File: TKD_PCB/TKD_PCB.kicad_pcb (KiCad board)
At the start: 2 copper layers, 83.8 x 53.3 mm, 3 parts, among them U1 ESP32-WROOM-32D

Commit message: Begin of the final assembly
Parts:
- removed D1, D3: LED, LED_THT:LED_D3.0mm
- removed U1: ESP32-WROOM-32D, RF_Module:ESP32-WROOM-32
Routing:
- net GND: track 35.9 -> 0.00 mm
- removed copper zone on F.Cu, net GND
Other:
- board outline removed

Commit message: did Remco's homework
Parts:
- added C1: 100nF, Capacitor_SMD:C_0805_2012Metric_Pad1.15x1.40mm_HandSolder, F.Cu at (38.5, 125.3)
- added C10: 100nF, Capacitor_SMD:C_0805_2012Metric_Pad1.15x1.40mm_HandSolder, F.Cu at (156.2, 102.5)
- added C11: 10uF, Capacitor_SMD:C_0805_2012Metric_Pad1.15x1.40mm_HandSolder, F.Cu at (150.5, 95.8)
- added C12: 100nF, Capacitor_SMD:C_0805_2012Metric_Pad1.15x1.40mm_HandSolder, F.Cu at (59.4, 147.7)
- added C13: 100nF, Capacitor_SMD:C_0805_2012Metric_Pad1.15x1.40mm_HandSolder, F.Cu at (59.5, 144.6)
- added C14: 100nF, Capacitor_SMD:C_0805_2012Metric_Pad1.15x1.40mm_HandSolder, F.Cu at (58.7, 169.2)
- added C15: 100nF, Capacitor_SMD:C_0805_2012Metric_Pad1.15x1.40mm_HandSolder, F.Cu at (48.4, 163.3)
- added C16: 100nF, Capacitor_SMD:C_0805_2012Metric_Pad1.15x1.40mm_HandSolder, F.Cu at (39.9, 154.8)
- added C17: 100nF, Capacitor_SMD:C_0805_2012Metric_Pad1.15x1.40mm_HandSolder, F.Cu at (34.0, 144.5)
- added C18: 100nF, Capacitor_SMD:C_0805_2012Metric_Pad1.15x1.40mm_HandSolder, F.Cu at (30.9, 133.0)
- added C19: 100nF, Capacitor_SMD:C_0805_2012Metric_Pad1.15x1.40mm_HandSolder, F.Cu at (30.9, 121.0)
- added C2: 10uF, Capacitor_SMD:C_0805_2012Metric_Pad1.15x1.40mm_HandSolder, F.Cu at (38.5, 127.7)
- added C20: 100nF, Capacitor_SMD:C_0805_2012Metric_Pad1.15x1.40mm_HandSolder, F.Cu at (34.0, 109.5)
- added C21: 100nF, Capacitor_SMD:C_0805_2012Metric_Pad1.15x1.40mm_HandSolder, F.Cu at (39.9, 99.2)
- added C22: 100nF, Capacitor_SMD:C_0805_2012Metric_Pad1.15x1.40mm_HandSolder, F.Cu at (48.4, 90.7)
- added C23: 100nF, Capacitor_SMD:C_0805_2012Metric_Pad1.15x1.40mm_HandSolder, F.Cu at (58.7, 84.8)
- added C24: 100nF, Capacitor_SMD:C_0805_2012Metric_Pad1.15x1.40mm_HandSolder, F.Cu at (70.2, 81.7)
- added C25: 100nF, Capacitor_SMD:C_0805_2012Metric_Pad1.15x1.40mm_HandSolder, F.Cu at (82.2, 81.7)
- added C26: 100nF, Capacitor_SMD:C_0805_2012Metric_Pad1.15x1.40mm_HandSolder, F.Cu at (93.7, 84.8)
- added C27: 100nF, Capacitor_SMD:C_0805_2012Metric_Pad1.15x1.40mm_HandSolder, F.Cu at (104.0, 90.7)
- added C28: 100nF, Capacitor_SMD:C_0805_2012Metric_Pad1.15x1.40mm_HandSolder, F.Cu at (112.5, 99.2)
- added C29: 100nF, Capacitor_SMD:C_0805_2012Metric_Pad1.15x1.40mm_HandSolder, F.Cu at (118.4, 109.5)
- added C3: 10uF, Capacitor_SMD:C_0805_2012Metric_Pad1.15x1.40mm_HandSolder, F.Cu at (89.8, 145.7)
- added C30: 100nF, Capacitor_SMD:C_0805_2012Metric_Pad1.15x1.40mm_HandSolder, F.Cu at (121.5, 121.0)
- added C31: 100nF, Capacitor_SMD:C_0805_2012Metric_Pad1.15x1.40mm_HandSolder, F.Cu at (121.5, 133.0)
- added C32: 100nF, Capacitor_SMD:C_0805_2012Metric_Pad1.15x1.40mm_HandSolder, F.Cu at (118.4, 144.5)
- added C33: 100nF, Capacitor_SMD:C_0805_2012Metric_Pad1.15x1.40mm_HandSolder, F.Cu at (112.5, 154.8)
- added C34: 100nF, Capacitor_SMD:C_0805_2012Metric_Pad1.15x1.40mm_HandSolder, F.Cu at (104.0, 163.3)
- added C35: 100nF, Capacitor_SMD:C_0805_2012Metric_Pad1.15x1.40mm_HandSolder, F.Cu at (93.7, 169.2)
- added C36: 100nF, Capacitor_SMD:C_0805_2012Metric_Pad1.15x1.40mm_HandSolder, F.Cu at (82.2, 172.3)
- added C37: 100nF, Capacitor_SMD:C_0805_2012Metric_Pad1.15x1.40mm_HandSolder, F.Cu at (70.2, 172.3)
- added C4: 100nF, Capacitor_SMD:C_0805_2012Metric_Pad1.15x1.40mm_HandSolder, F.Cu at (89.7, 143.4)
- added C5: 100nF, Capacitor_SMD:C_0805_2012Metric_Pad1.15x1.40mm_HandSolder, F.Cu at (89.6, 148.8)
- added C6: 10uF, Capacitor_SMD:C_0805_2012Metric_Pad1.15x1.40mm_HandSolder, F.Cu at (89.6, 151.9)
- added C7: 100nF, Capacitor_SMD:C_0805_2012Metric_Pad1.15x1.40mm_HandSolder, F.Cu at (59.6, 141.3)
- added C8: 10uF, Capacitor_SMD:C_0805_2012Metric_Pad1.15x1.40mm_HandSolder, F.Cu at (155.8, 98.2)
- added C9: 100nF, Capacitor_SMD:C_0805_2012Metric_Pad1.15x1.40mm_HandSolder, F.Cu at (89.7, 139.8)
- added D1: D, Diode_SMD:D_0805_2012Metric_Pad1.15x1.40mm_HandSolder, F.Cu at (100.1, 151.2)
- added D10: WS2812B, LED_SMD:LED_WS2812B_PLCC4_5.0x5.0mm_P3.2mm, F.Cu at (43.9, 159.3)
- added D11: WS2812B, LED_SMD:LED_WS2812B_PLCC4_5.0x5.0mm_P3.2mm, F.Cu at (36.6, 149.9)
- added D12: WS2812B, LED_SMD:LED_WS2812B_PLCC4_5.0x5.0mm_P3.2mm, F.Cu at (32.0, 138.8)
- added D13: WS2812B, LED_SMD:LED_WS2812B_PLCC4_5.0x5.0mm_P3.2mm, F.Cu at (30.5, 127.0)
- added D14: WS2812B, LED_SMD:LED_WS2812B_PLCC4_5.0x5.0mm_P3.2mm, F.Cu at (32.0, 115.2)
- added D15: WS2812B, LED_SMD:LED_WS2812B_PLCC4_5.0x5.0mm_P3.2mm, F.Cu at (36.6, 104.1)
- added D16: WS2812B, LED_SMD:LED_WS2812B_PLCC4_5.0x5.0mm_P3.2mm, F.Cu at (43.9, 94.7)
- added D17: WS2812B, LED_SMD:LED_WS2812B_PLCC4_5.0x5.0mm_P3.2mm, F.Cu at (53.3, 87.4)
- added D18: WS2812B, LED_SMD:LED_WS2812B_PLCC4_5.0x5.0mm_P3.2mm, F.Cu at (64.4, 82.8)
- added D19: WS2812B, LED_SMD:LED_WS2812B_PLCC4_5.0x5.0mm_P3.2mm, F.Cu at (76.2, 81.3)
- added D2: D, Diode_SMD:D_SOD-123, F.Cu at (38.7, 119.8)
- added D20: WS2812B, LED_SMD:LED_WS2812B_PLCC4_5.0x5.0mm_P3.2mm, F.Cu at (88.0, 82.8)
- added D21: WS2812B, LED_SMD:LED_WS2812B_PLCC4_5.0x5.0mm_P3.2mm, F.Cu at (99.1, 87.4)
- added D22: WS2812B, LED_SMD:LED_WS2812B_PLCC4_5.0x5.0mm_P3.2mm, F.Cu at (108.5, 94.7)
- added D23: WS2812B, LED_SMD:LED_WS2812B_PLCC4_5.0x5.0mm_P3.2mm, F.Cu at (115.8, 104.1)
- added D24: WS2812B, LED_SMD:LED_WS2812B_PLCC4_5.0x5.0mm_P3.2mm, F.Cu at (120.4, 115.2)
- added D25: WS2812B, LED_SMD:LED_WS2812B_PLCC4_5.0x5.0mm_P3.2mm, F.Cu at (121.9, 127.0)
- added D26: WS2812B, LED_SMD:LED_WS2812B_PLCC4_5.0x5.0mm_P3.2mm, F.Cu at (120.4, 138.8)
- added D27: WS2812B, LED_SMD:LED_WS2812B_PLCC4_5.0x5.0mm_P3.2mm, F.Cu at (115.8, 149.9)
- added D28: WS2812B, LED_SMD:LED_WS2812B_PLCC4_5.0x5.0mm_P3.2mm, F.Cu at (108.5, 159.3)
- added D29: WS2812B, LED_SMD:LED_WS2812B_PLCC4_5.0x5.0mm_P3.2mm, F.Cu at (99.1, 166.6)
- added D3: LED, Diode_SMD:D_0805_2012Metric_Pad1.15x1.40mm_HandSolder, F.Cu at (95.6, 155.2)
- added D30: WS2812B, LED_SMD:LED_WS2812B_PLCC4_5.0x5.0mm_P3.2mm, F.Cu at (88.0, 171.2)
- added D4: D, Diode_SMD:D_0805_2012Metric_Pad1.15x1.40mm_HandSolder, F.Cu at (155.5, 88.4)
- added D5: LED, Diode_SMD:D_0805_2012Metric_Pad1.15x1.40mm_HandSolder, F.Cu at (156.4, 93.1)
- added D6: D, Diode_SMD:D_0805_2012Metric_Pad1.15x1.40mm_HandSolder, F.Cu at (59.4, 136.5)
- added D7: WS2812B, LED_SMD:LED_WS2812B_PLCC4_5.0x5.0mm_P3.2mm, F.Cu at (76.2, 172.7)
- added D8: WS2812B, LED_SMD:LED_WS2812B_PLCC4_5.0x5.0mm_P3.2mm, F.Cu at (64.4, 171.2)
- added D9: WS2812B, LED_SMD:LED_WS2812B_PLCC4_5.0x5.0mm_P3.2mm, F.Cu at (53.3, 166.6)
- added IC1: R5460N233AF-TR-FE, SamacSys_Parts:SOT95P280X140-6N, F.Cu at (54.1, 143.5)
- added J2: Conn_01x06, Connector_PinSocket_2.54mm:PinSocket_1x06_P2.54mm_Vertical, F.Cu at (84.1, 124.5)
- added J3: Conn_02x02_Top_Bottom, Connector_PinHeader_2.54mm:PinHeader_2x02_P2.54mm_Vertical, F.Cu at (54.8, 96.5)
- added J4: Conn_01x07, Connector_PinSocket_2.54mm:PinSocket_1x07_P2.54mm_Vertical, F.Cu at (99.0, 100.2)
- added J5: Conn_01x08, Connector_PinSocket_2.54mm:PinSocket_1x08_P2.54mm_Vertical, F.Cu at (60.8, 100.2)
- added Q1: ZXMN6A09GQTA, SamacSys_Parts:SOT230P700X165-4N, F.Cu at (45.1, 145.6)
- added Q2: ZXMN6A09GQTA, SamacSys_Parts:SOT230P700X165-4N, F.Cu at (45.1, 138.5)
- added Q3: S8050, Package_TO_SOT_THT:TO-92_Inline, F.Cu at (54.4, 125.0)
- added Q4: S8050, Package_TO_SOT_THT:TO-92_Inline, F.Cu at (54.5, 132.2)
- added R1: 22R, Resistor_SMD:R_0805_2012Metric_Pad1.15x1.40mm_HandSolder, F.Cu at (55.5, 116.7)
- added R10: 12k, Resistor_SMD:R_0805_2012Metric_Pad1.15x1.40mm_HandSolder, F.Cu at (55.4, 128.3)
- added R11: 10k, Resistor_SMD:R_0805_2012Metric_Pad1.15x1.40mm_HandSolder, F.Cu at (60.8, 126.3)
- added R12: 5k, Resistor_SMD:R_0805_2012Metric_Pad1.15x1.40mm_HandSolder, F.Cu at (89.7, 121.0)
- added R2: 1k, Resistor_SMD:R_0805_2012Metric_Pad1.15x1.40mm_HandSolder, F.Cu at (95.8, 151.7)
- added R3: 22R, Resistor_SMD:R_0805_2012Metric_Pad1.15x1.40mm_HandSolder, F.Cu at (55.5, 118.7)
- added R4: 330R, Resistor_SMD:R_0805_2012Metric_Pad1.15x1.40mm_HandSolder, F.Cu at (59.5, 138.7)
- added R5: 1k, Resistor_SMD:R_0805_2012Metric_Pad1.15x1.40mm_HandSolder, F.Cu at (54.1, 147.7)
- added R6: 330R, Resistor_SMD:R_0805_2012Metric_Pad1.15x1.40mm_HandSolder, F.Cu at (54.1, 138.6)
- added R7: 1k, Resistor_SMD:R_0805_2012Metric_Pad1.15x1.40mm_HandSolder, F.Cu at (146.1, 92.2)
- added R8: 12k, Resistor_SMD:R_0805_2012Metric_Pad1.15x1.40mm_HandSolder, F.Cu at (55.8, 121.2)
- added R9: 10k, Resistor_SMD:R_0805_2012Metric_Pad1.15x1.40mm_HandSolder, F.Cu at (60.7, 123.0)
- added SW1: SW_Push, Button_Switch_THT:SW_PUSH_6mm, F.Cu at (44.4, 104.1)
- added SW2: SW_Push, Button_Switch_THT:SW_PUSH_6mm, F.Cu at (44.4, 111.7)
- added SW3: SW_SPDT, SamacSys_Parts:AYZ0103AGRLC, F.Cu at (75.0, 168.3)
- added U1: AMS1117-3.3, Package_TO_SOT_SMD:SOT-223-3_TabPin2, F.Cu at (98.2, 145.4)
- added U2: FT232RL, Package_SO:SSOP-28_5.3x10.2mm_P0.65mm, F.Cu at (45.6, 125.9)
- added U3: LM1085-5.0, Package_TO_SOT_SMD:TO-263-3_TabPin4, F.Cu at (168.7, 98.7)
- added U4: ESP32-WROOM-32D, RF_Module:ESP32-WROOM-32, F.Cu at (77.0, 107.3)
- added U5: 1049, SamacSys_Parts:1049, B.Cu at (75.8, 127.7)
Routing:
- net Batt_1_GND: track 0.00 -> 35.3 mm, vias 0 -> 2
- net /EN: track 0.00 -> 28.7 mm
- net /HSPIMOSI: track 0.00 -> 28.3 mm, vias 0 -> 1
- net Net-(C12-Pad2): track 0.00 -> 22.1 mm
- net +5V: track 0.00 -> 20.6 mm
- net /GPIO15: track 0.00 -> 20.4 mm, vias 0 -> 1
- net Net-(Q1-Pad2): track 0.00 -> 19.2 mm
- net /GPIO17: track 0.00 -> 16.2 mm
- net /GPIO16: track 0.00 -> 15.7 mm
- net /GPIO22: track 0.00 -> 15.3 mm
- net /GPIO4: track 0.00 -> 15.1 mm
- net /GPIO21: track 0.00 -> 14.6 mm
- net Batt_1_+: track 0.00 -> 14.0 mm
- net Net-(C13-Pad1): track 0.00 -> 10.5 mm
- net Net-(C7-Pad2): track 0.00 -> 10.1 mm
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- added copper zone on B.Cu, net Batt_2_GND
- added copper zone on F.Cu, net Batt_2_GND
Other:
- board outline added: 100 x 100 mm

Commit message: some more routing
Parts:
- added J1: USB2066-05-RBHM-15-STB-00-00-A, SamacSys_Parts:USB206605RBHM15STB0000A, B.Cu at (30.4, 125.9)
- moved D10 91.4 mm to (108.5, 94.7), turned to 135 degrees
- moved D16 91.4 mm to (108.5, 159.3), turned to 45 degrees
- moved D22 91.4 mm to (43.9, 159.3), turned to 315 degrees
- moved D28 91.4 mm to (43.9, 94.7), turned to 225 degrees
- moved C18 91.4 mm to (121.5, 121.0)
- moved C19 91.4 mm to (121.5, 133.0)
- moved C24 91.4 mm to (82.2, 172.3)
- moved C25 91.4 mm to (70.2, 172.3)
- moved C30 91.4 mm to (30.9, 133.0)
- moved C31 91.4 mm to (30.9, 121.0)
- moved C36 91.4 mm to (70.2, 81.7)
- moved C37 91.4 mm to (82.2, 81.7)
- moved D17 91.4 mm to (99.1, 166.6), turned to 30 degrees
- moved D29 91.4 mm to (53.3, 87.4), turned to 210 degrees
- moved D11 91.4 mm to (115.8, 104.1), turned to 120 degrees
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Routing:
- net /GPIO0: track 6.50 -> 46.2 mm, vias 0 -> 1
- net /TXD0: track 1.51 -> 39.4 mm, vias 0 -> 2
- net /RXD0: track 1.53 -> 37.9 mm, vias 0 -> 2
- net Net-(D6-Pad2): track 0.00 -> 32.4 mm
- net +5V: track 20.6 -> 49.3 mm
- net /Fastled_Pin: track 2.86 -> 30.5 mm
- net Batt_1_GND: track 35.3 -> 16.2 mm
- net Net-(Q3-Pad2): track 0.00 -> 14.0 mm
- net Net-(R1-Pad2): track 0.00 -> 13.5 mm, vias 0 -> 2
- net Net-(Q4-Pad1): track 0.00 -> 11.8 mm
- net Net-(Q3-Pad1): track 0.00 -> 10.9 mm
- net Net-(J1-Pad3): track 0.00 -> 10.2 mm, vias 0 -> 1
- net Net-(J1-Pad2): track 0.00 -> 9.93 mm, vias 0 -> 1
- net Batt_2_GND: track 0.00 -> 9.37 mm, vias 3 -> 6
- net Net-(U2-Pad17): track 0.00 -> 9.35 mm
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
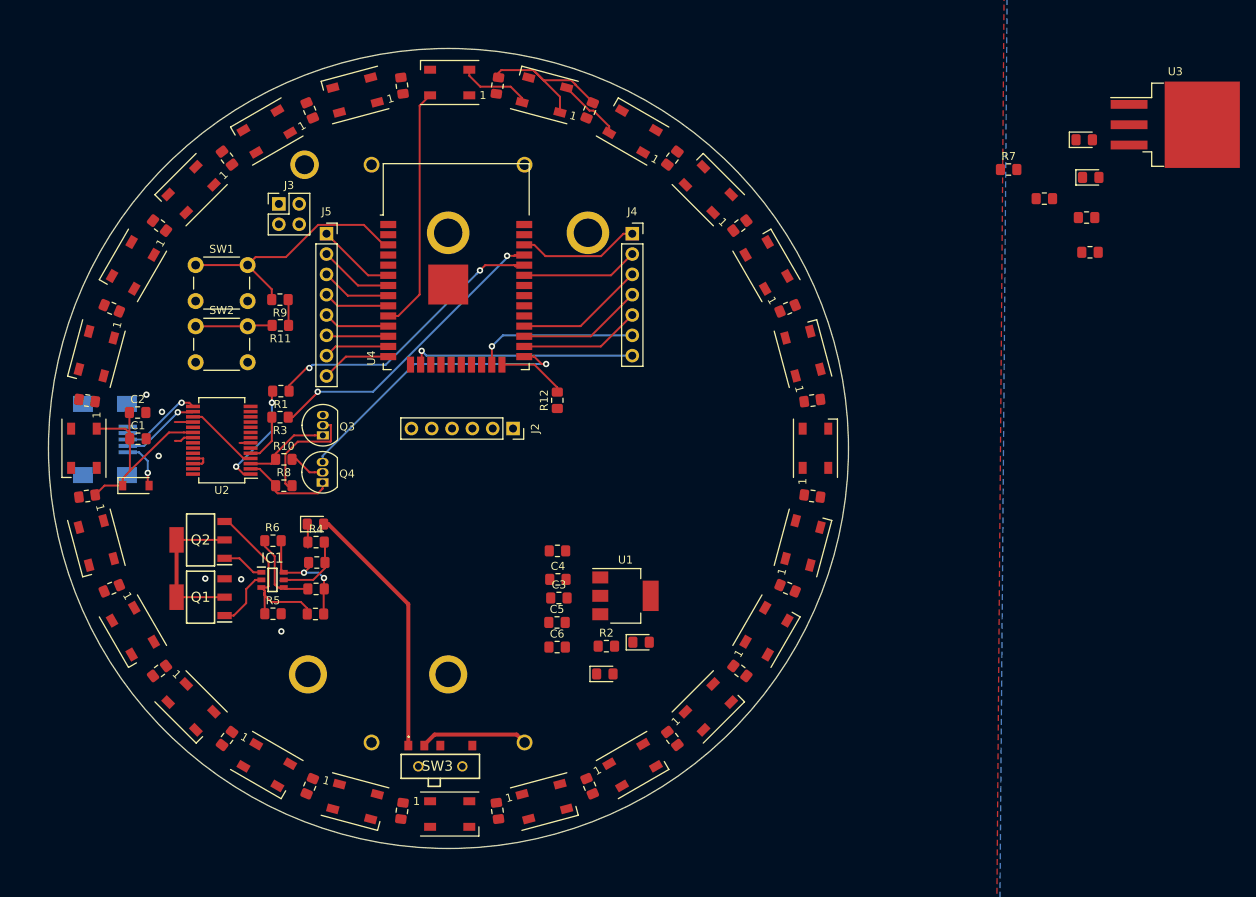
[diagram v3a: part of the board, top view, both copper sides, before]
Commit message: made PCB smaller
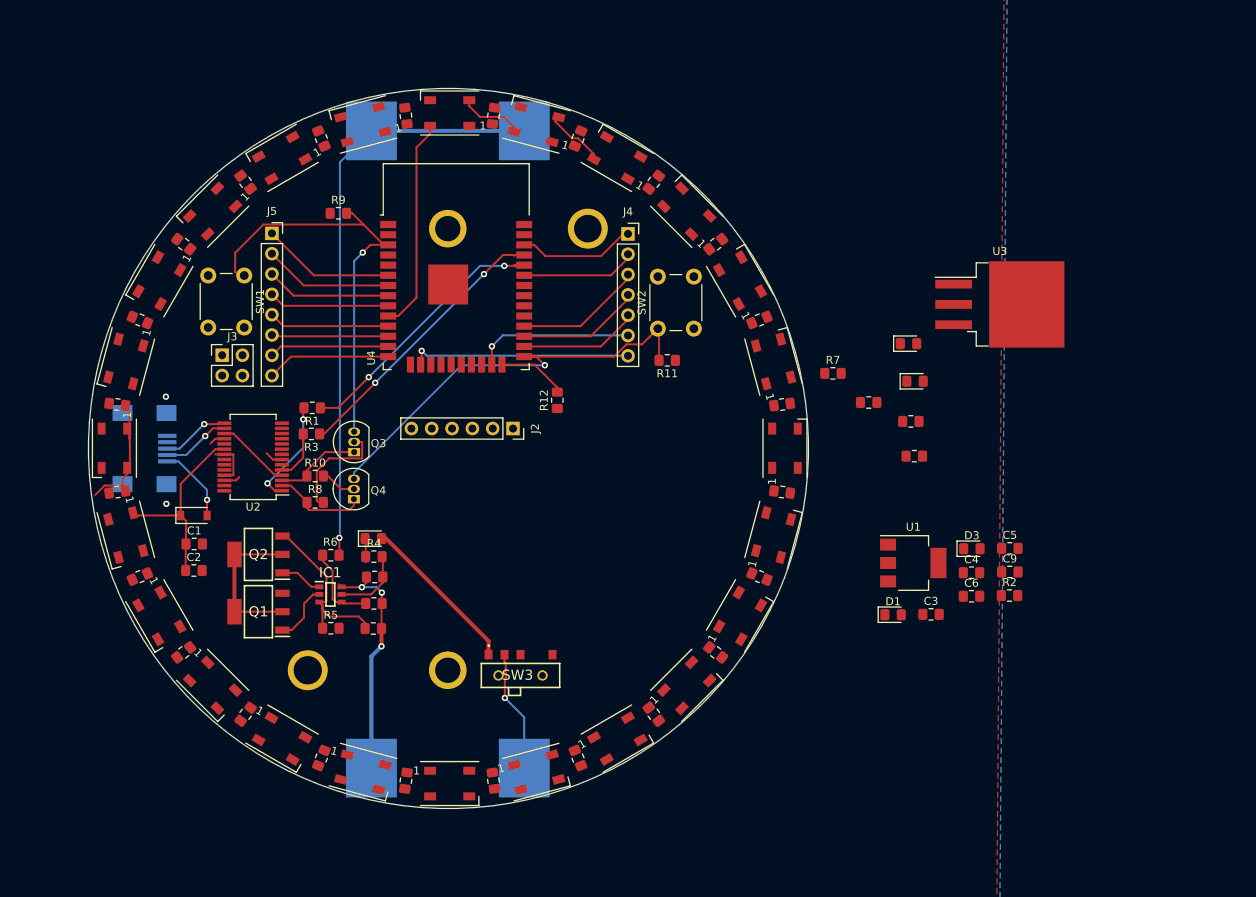
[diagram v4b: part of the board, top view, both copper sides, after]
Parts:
- U5: value 1049 -> 1048; footprint SamacSys_Parts:1049 -> SamacSys_Parts:1048
- moved SW2 57.8 mm to (102.2, 112.0), turned to 90 degrees
- moved C5 57.4 mm to (146.2, 139.5)
- moved C9 56.6 mm to (146.2, 142.5)
- moved C6 52.2 mm to (141.4, 145.5)
- moved C4 51.7 mm to (141.4, 142.5)
- moved R2 50.8 mm to (146.2, 145.4)
- moved R11 48.6 mm to (103.4, 116.0)
- moved D3 48.5 mm to (141.5, 139.6)
- moved C3 46.6 mm to (136.4, 147.8)
- moved U1 36.2 mm to (134.1, 141.3)
- moved C8 33.6 mm to (133.8, 123.6)
- moved C10 33.6 mm to (134.3, 128.0)
- moved C11 33.6 mm to (128.6, 121.3)
- moved R7 33.6 mm to (124.1, 117.6)
- moved D4 33.6 mm to (133.6, 113.9)
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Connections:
- C1 pad 2: Batt_2_GND -> GND
- C10 pad 2: Batt_2_GND -> GND
- C11 pad 2: Batt_2_GND -> GND
- C14 pad 2: Batt_2_GND -> GND
- C15 pad 2: Batt_2_GND -> GND
- C16 pad 2: Batt_2_GND -> GND
- C17 pad 2: Batt_2_GND -> GND
- C18 pad 2: Batt_2_GND -> GND
- C19 pad 2: Batt_2_GND -> GND
- C2 pad 2: Batt_2_GND -> GND
- C20 pad 2: Batt_2_GND -> GND
- C21 pad 2: Batt_2_GND -> GND
- C22 pad 2: Batt_2_GND -> GND
- C23 pad 2: Batt_2_GND -> GND
- C24 pad 2: Batt_2_GND -> GND
- C25 pad 2: Batt_2_GND -> GND
- C26 pad 2: Batt_2_GND -> GND
- C27 pad 2: Batt_2_GND -> GND
- C28 pad 2: Batt_2_GND -> GND
- C29 pad 2: Batt_2_GND -> GND
- C3 pad 2: Batt_2_GND -> GND
- C30 pad 2: Batt_2_GND -> GND
- C31 pad 2: Batt_2_GND -> GND
- C32 pad 2: Batt_2_GND -> GND
- C33 pad 2: Batt_2_GND -> GND
- C34 pad 2: Batt_2_GND -> GND
- C35 pad 2: Batt_2_GND -> GND
- C36 pad 2: Batt_2_GND -> GND
- C37 pad 2: Batt_2_GND -> GND
- C4 pad 1: Batt_2_GND -> GND
- C5 pad 2: Batt_2_GND -> GND
- C6 pad 2: Batt_2_GND -> GND
- C8 pad 2: Batt_2_GND -> GND
- C9 pad 1: Batt_2_GND -> GND
- D10 pad 3: Batt_2_GND -> GND
- D11 pad 3: Batt_2_GND -> GND
- D12 pad 3: Batt_2_GND -> GND
- D13 pad 3: Batt_2_GND -> GND
- D14 pad 3: Batt_2_GND -> GND
- D15 pad 3: Batt_2_GND -> GND
- D16 pad 3: Batt_2_GND -> GND
- D17 pad 3: Batt_2_GND -> GND
- D18 pad 3: Batt_2_GND -> GND
- D19 pad 3: Batt_2_GND -> GND
- D20 pad 3: Batt_2_GND -> GND
- D21 pad 3: Batt_2_GND -> GND
- D22 pad 3: Batt_2_GND -> GND
- D23 pad 3: Batt_2_GND -> GND
- D24 pad 3: Batt_2_GND -> GND
- D25 pad 3: Batt_2_GND -> GND
- D26 pad 3: Batt_2_GND -> GND
- D27 pad 3: Batt_2_GND -> GND
- D28 pad 3: Batt_2_GND -> GND
- D29 pad 3: Batt_2_GND -> GND
- D3 pad 1: Batt_2_GND -> GND
- D30 pad 3: Batt_2_GND -> GND
- D5 pad 1: Batt_2_GND -> GND
- D7 pad 3: Batt_2_GND -> GND
- D8 pad 3: Batt_2_GND -> GND
- D9 pad 3: Batt_2_GND -> GND
- J1 pad 5: Batt_2_GND -> GND
- J1 pad MP1: Batt_2_GND -> GND
- J1 pad MP2: Batt_2_GND -> GND
- J1 pad MP3: Batt_2_GND -> GND
- J1 pad MP4: Batt_2_GND -> GND
- J2 pad 6: Batt_2_GND -> GND
- J3 pad 3: Batt_2_GND -> GND
- J3 pad 4: Batt_2_GND -> GND
- Q1 pad 3: Batt_2_GND -> GND
- R12 pad 1: Batt_2_GND -> GND
- R5 pad 2: Batt_2_GND -> GND
- R6 pad 1: Batt_1_GND -> Batt_1_+
- SW1 pad 2: Batt_2_GND -> GND
- SW2 pad 2: Batt_2_GND -> GND
- SW3 pad 2: Batt_1_+ -> Batt_2_+
- U1 pad 1: Batt_2_GND -> GND
- U2 pad 18: Batt_2_GND -> GND
- U2 pad 21: Batt_2_GND -> GND
- U2 pad 25: Batt_2_GND -> GND
- U2 pad 26: Batt_2_GND -> GND
- U2 pad 7: Batt_2_GND -> GND
- U3 pad 1: Batt_2_GND -> GND
- U4 pad 1: Batt_2_GND -> GND
- U4 pad 15: Batt_2_GND -> GND
- U4 pad 38: Batt_2_GND -> GND
- U4 pad 39: Batt_2_GND -> GND
- U5 pad 1: Net-(U5-Pad1) -> Batt_1_GND
- U5 pad 2: Net-(U5-Pad2) -> Batt_1_+
- U5 pad 3: Net-(U5-Pad3) -> Batt_1_+
- U5 pad 4: Net-(U5-Pad4) -> Batt_2_+
- U5 pad 5: Net-(U5-Pad5) -> (no net)
- U5 pad 6: Batt_2_GND -> (no net)
- U5 pad 7: Batt_1_+ -> (no net)
- U5 pad 9: Batt_1_GND -> (no net)
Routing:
- net Batt_1_+: track 13.6 -> 73.8 mm, vias 0 -> 1
- net /EN: track 32.8 -> 54.6 mm, vias 0 -> 1
- net Batt_2_+: track 0.00 -> 15.3 mm, vias 0 -> 1
- net Batt_1_GND: track 16.2 -> 30.6 mm, vias 2 -> 3
- net GND: track 0.00 -> 12.4 mm, vias 0 -> 2
- net Net-(D6-Pad2): track 32.4 -> 20.4 mm
- net +5V: track 49.3 -> 39.4 mm
- net Batt_2_GND: track 9.37 -> 0.00 mm, vias 6 -> 0
- net /GPIO0: track 46.2 -> 55.4 mm
- net /GPIO35: track 9.34 -> 16.2 mm
- net /GPIO34: track 9.87 -> 16.7 mm
- net /GPIO32: track 8.81 -> 15.7 mm
- net /GPIO26: track 8.29 -> 15.1 mm
- net /GPIO27: track 7.76 -> 14.6 mm
- net /GPIO33: track 8.29 -> 15.1 mm
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- added copper zone on B.Cu, net GND
- added copper zone on F.Cu, net GND
- removed copper zone on B.Cu, net Batt_2_GND
- removed copper zone on F.Cu, net Batt_2_GND
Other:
- board size 100 x 100 mm -> 90 x 90 mm

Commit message: Final check before ordering
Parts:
- removed J3: Conn_02x02_Top_Bottom, Connector_PinHeader_2.54mm:PinHeader_2x02_P2.54mm_Vertical
- C12, C13, C7, D2, D6, IC1, J2, Q1, Q2, R4, R5, R6, SW3: moved to B.Cu
- moved R2 78.1 mm to (68.1, 143.9), turned to 270 degrees
- moved D3 74.0 mm to (68.1, 149.2), turned to 90 degrees
- moved C5 71.5 mm to (74.8, 143.9), turned to 270 degrees
- moved C6 68.7 mm to (72.8, 143.9), turned to 270 degrees
- moved C4 64.0 mm to (77.5, 143.9), turned to 90 degrees
- moved Q1 62.1 mm to (113.7, 137.7), turned to 270 degrees
- moved D1 61.0 mm to (70.7, 143.9), turned to 90 degrees
- moved U3 59.5 mm to (89.9, 131.5), turned to 90 degrees
- moved D4 58.8 mm to (82.9, 143.9), turned to 90 degrees
- moved D5 58.0 mm to (85.2, 149.5), turned to 90 degrees
- moved U1 57.4 mm to (77.1, 135.4), turned to 90 degrees
- moved R5 57.0 mm to (112.4, 124.2)
- moved C3 56.9 mm to (79.6, 143.9), turned to 270 degrees
- moved Q2 54.1 mm to (106.3, 137.5), turned to 270 degrees
- moved C12 53.5 mm to (112.4, 121.8), turned to 0 degrees
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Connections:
- net /VSPIMISO renamed /VSPI_SDI
- net /VSPIMOSI renamed /VSPI_SDO
- C1 pad 1: +5V -> /USB_5V
- C2 pad 1: +5V -> /USB_5V
- D2 pad 2: Net-(D2-Pad2) -> /USB_5V
- J1 pad 1: Net-(D2-Pad2) -> /USB_5V
- U2 pad 20: +5V -> /USB_5V
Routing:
- net +5V: track 39.4 -> 324.5 mm, vias 0 -> 1
- net +3V3: track 0.00 -> 103.7 mm, vias 0 -> 3
- net /GPIO0: track 55.4 -> 109.6 mm, vias 1 -> 4
- net Batt_1_GND: track 30.6 -> 75.5 mm, vias 3 -> 0
- net /VSPICS: track 0.00 -> 39.6 mm, vias 0 -> 2
- net +BATT: track 2.98 -> 41.9 mm, vias 0 -> 2
- net Net-(Q4-Pad1): track 11.8 -> 47.1 mm
- net /VSPI_SDO: track 0.00 -> 33.3 mm, vias 0 -> 3
- net /VSPICLK: track 0.00 -> 30.3 mm, vias 0 -> 2
- net Net-(Q3-Pad1): track 10.9 -> 40.7 mm
- net /VSPI_SDI: track 0.00 -> 29.3 mm, vias 0 -> 2
- net Net-(IC1-Pad1): track 5.32 -> 33.7 mm
- net /USB_5V: track 0.00 -> 23.0 mm, vias 0 -> 1
- net GND: track 12.4 -> 31.7 mm, vias 2 -> 5
- net Net-(C5-Pad1): track 0.00 -> 18.3 mm
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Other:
- net class Default: clearance 0.13 -> 0.2; trace_width 0.25 -> 0.128
- rule trace_clearance: 0.13 -> 0.2
- rule trace_min: 0.2 -> 0.128
- rule via_min_size: 0.4 -> 0.6
